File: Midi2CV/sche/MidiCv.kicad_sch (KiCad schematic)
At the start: 9 parts, among them U1 STM32F103C8T6_BD, U2 6N138

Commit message: re - revert
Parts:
- added U3: ~, symbol RetroElec:MCP4725_DAC_BD
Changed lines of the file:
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@@
+    )
+  )
+  (symbol (lib_id "RetroElec:MCP4725_DAC_BD") (at 195.58 54.61 0) (unit 1)
+    (in_bom yes) (on_board yes) (dnp no) (fields_autoplaced)
+    (property "Reference" "U3" (at 205.74 52.8292 0)
+      (effects (font (size 1.27 1.27)) (justify left))
+    )
+    (property "Value" "~" (at 194.31 52.07 0)
+      (effects (font (size 1.27 1.27)))
+    )
+    (property "Footprint" "" (at 194.31 52.07 0)
+      (effects (font (size 1.27 1.27)) hide)
+    )
+    (property "Datasheet" "" (at 194.31 52.07 0)
+      (effects (font (size 1.27 1.27)) hide)
+    )
+    (pin "")
+    (pin "")
+    (pin "")
+    (pin "")
+    (pin "")
+    (pin "")
+    (instances
+      (project "MidiCv"
+        (path "/0e81e7e9-28eb-4e3c-9e5d-03b0357b6be8"
+          (reference "U3") (unit 1)
+        )
+      )
     )
   )

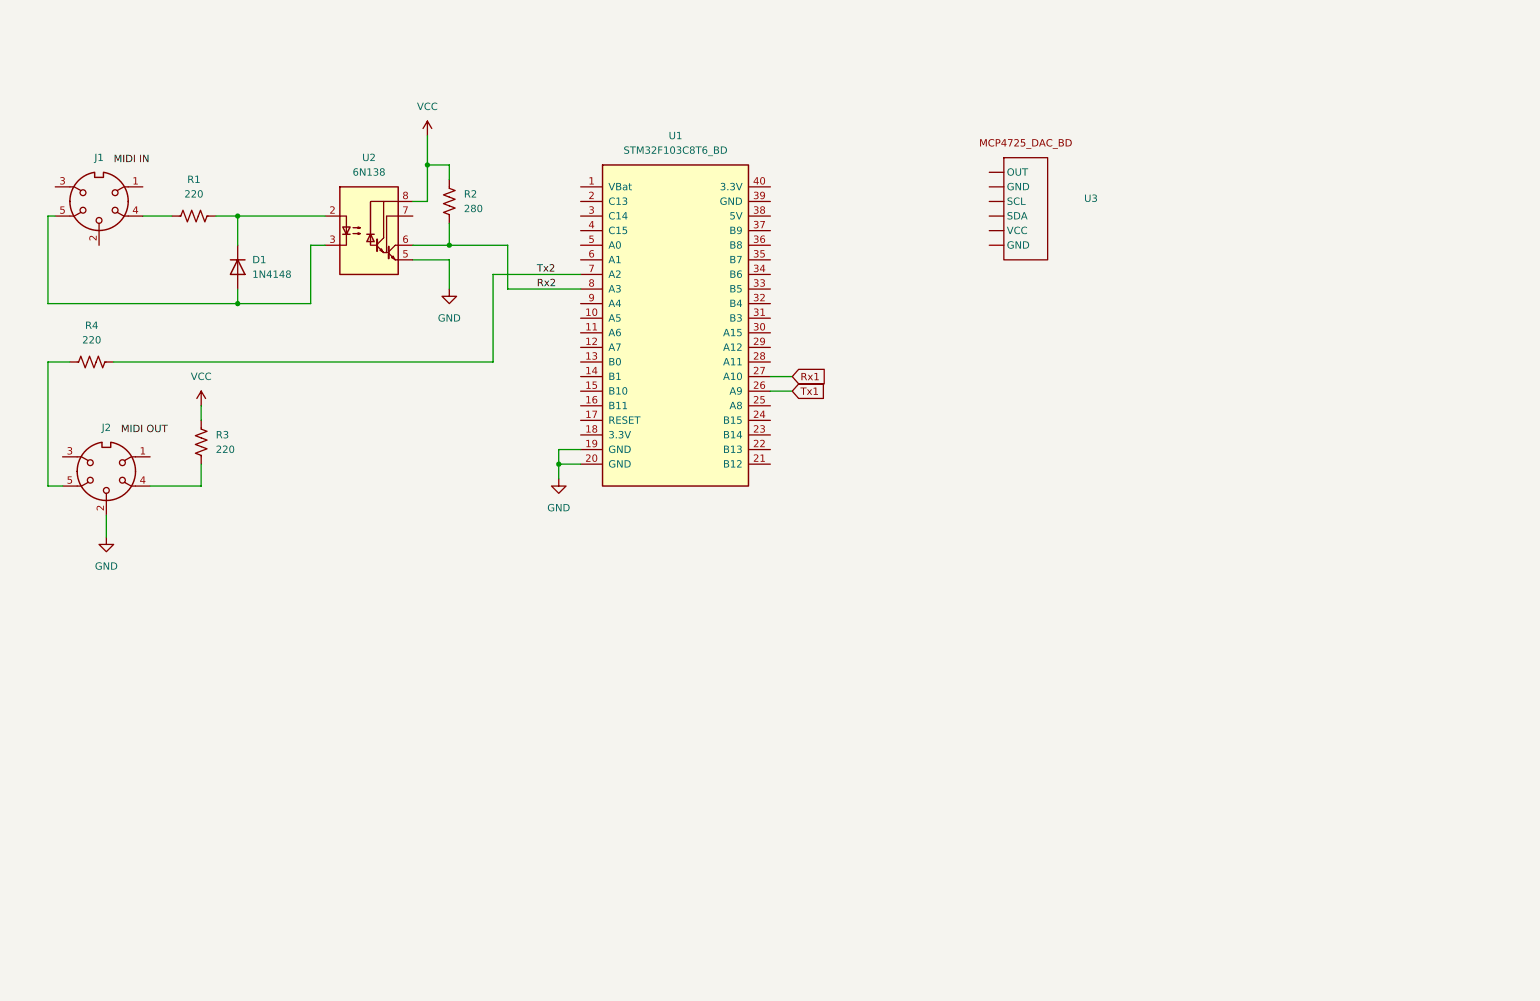
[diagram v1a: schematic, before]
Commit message: add i2c, A0_sel_pin
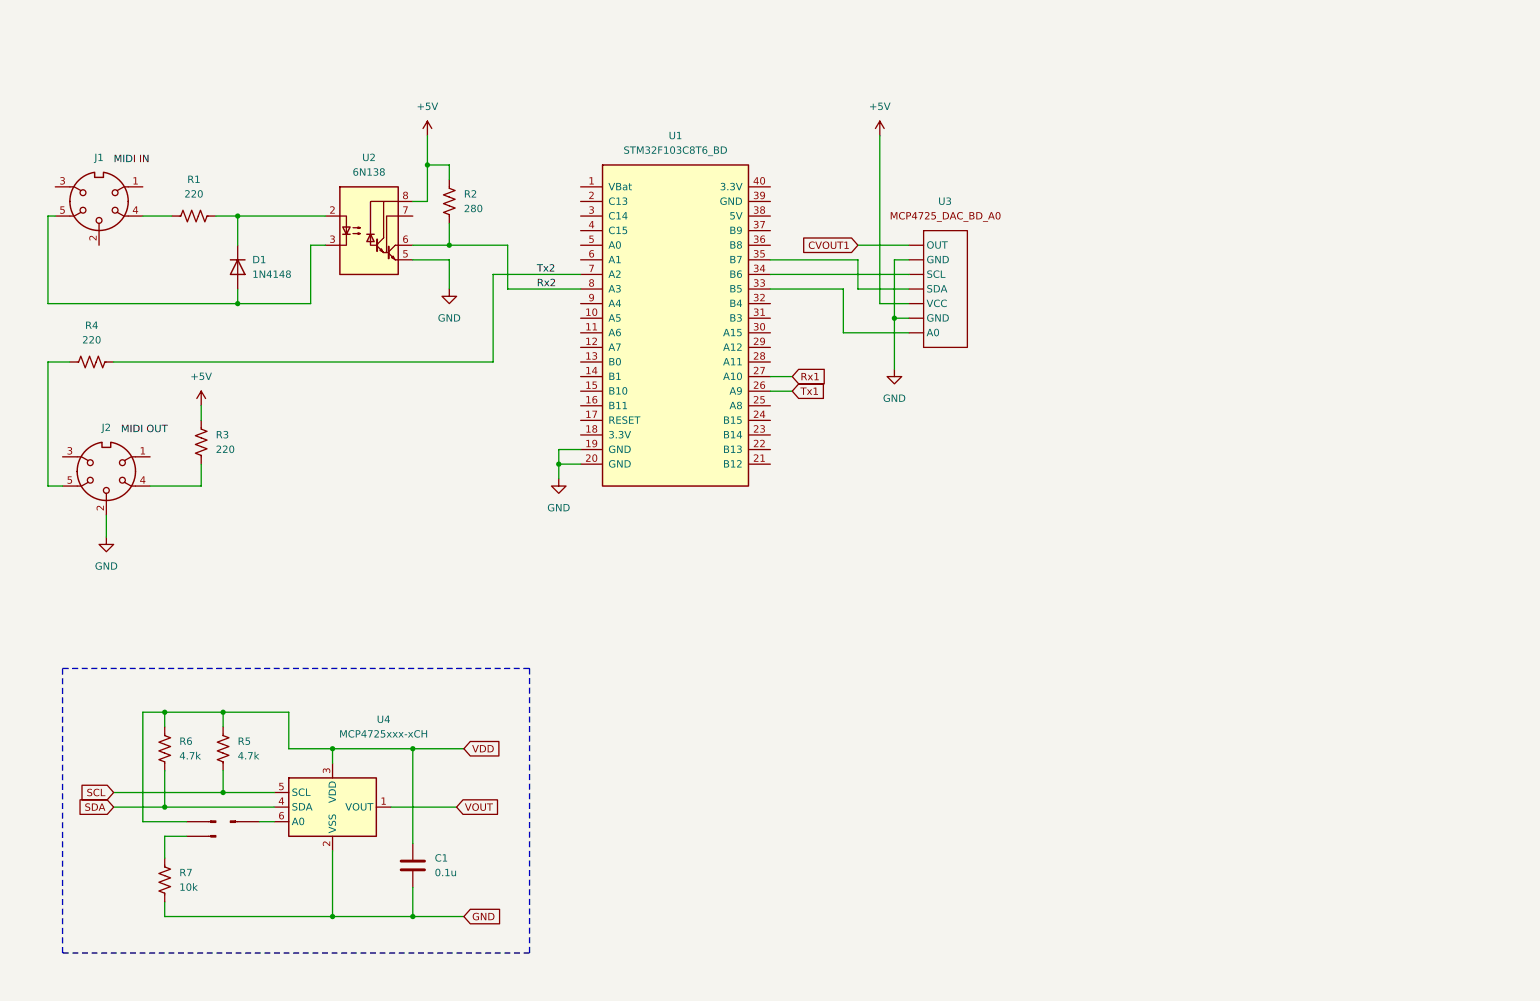
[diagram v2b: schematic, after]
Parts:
- removed U3: ~, symbol RetroElec:MCP4725_DAC_BD
- added C1: 0.1u, symbol Device:C
- added J3, J4, J5: Conn_01x01_Pin, symbol Connector:Conn_01x01_Pin
- added R5, R6: 4.7k, symbol Device:R_US
- added R7: 10k, symbol Device:R_US
- added U3: ~, symbol RetroElec:MCP4725_DAC_BD_A0
- added U4: MCP4725xxx-xCH, Package_TO_SOT_SMD:SOT-23-6, symbol Analog_DAC:MCP4725xxx-xCH
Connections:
- net GND: now also C1.2, R7.1, U3. (VCC), U4.2 (VSS)
- net at U1.33 (B5): now also U3. (VCC)
- net at U1.34 (B6): now also U3. (VCC)
- net at U1.35 (B7): now also U3. (VCC)
- net VCC renamed +5V
- net +5V: now also U3. (VCC)
- new net: J4.1 (Pin_1), U4.6 (A0)
- new net: J3.1 (Pin_1), R7.2
- new net CVOUT1: U3. (VCC)
- new net SCL: R5.1, U4.5 (SCL)
- new net SDA: R6.1, U4.4 (SDA)
- new net VDD: C1.1, J5.1 (Pin_1), R5.2, R6.2, U4.3 (VDD)
- new net VOUT: U4.1 (VOUT)

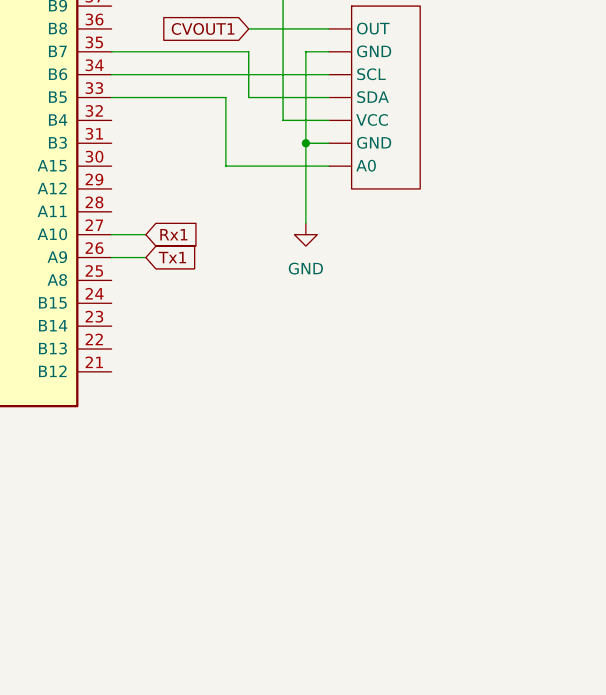
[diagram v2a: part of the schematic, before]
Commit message: - add set_CV function - add GATE control
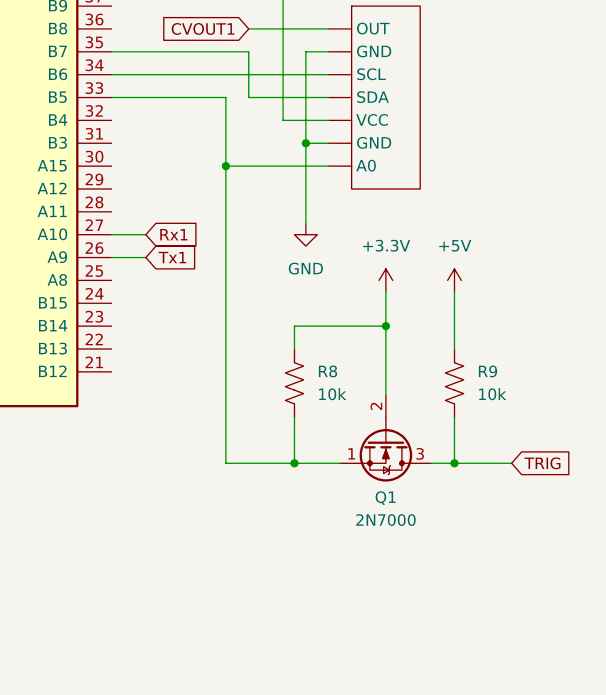
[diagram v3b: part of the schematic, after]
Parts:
- added Q1: 2N7000, Package_TO_SOT_THT:TO-92_Inline, symbol Transistor_FET:2N7000
- added R8, R9: 10k, symbol Device:R_US
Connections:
- net +5V: now also R9.2
- net at U1.33 (B5), U3. (VCC): now also Q1.1 (S), R8.1
- new net +3.3V: Q1.2 (G), R8.2
- new net TRIG: Q1.3 (D), R9.1
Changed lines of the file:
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@@
   (junction (at 74.93 148.59) (diameter 0) (color 0 0 0 0)
   )
+  (junction (at 181.61 93.98) (diameter 0) (color 0 0 0 0)
+  )
   (junction (at 55.88 142.24) (diameter 0) (color 0 0 0 0)
   )
@@
   (junction (at 91.44 46.99) (diameter 0) (color 0 0 0 0)
   )
+  (junction (at 163.83 76.2) (diameter 0) (color 0 0 0 0)
+  )
   (junction (at 74.93 177.8) (diameter 0) (color 0 0 0 0)
   )
@@
   (junction (at 45.72 142.24) (diameter 0) (color 0 0 0 0)
   )
+  (junction (at 171.45 109.22) (diameter 0) (color 0 0 0 0)
+  )
   (junction (at 172.72 73.66) (diameter 0) (color 0 0 0 0)
   )
@@
   (junction (at 114.3 99.06) (diameter 0) (color 0 0 0 0)
   )
+  (junction (at 189.23 109.22) (diameter 0) (color 0 0 0 0)
+  )
   (junction (at 45.72 158.75) (diameter 0) (color 0 0 0 0)
   )
@@
     (stroke (width 0) (type default))
   )
+  (wire (pts (xy 171.45 109.22) (xy 176.53 109.22))
+    (stroke (width 0) (type default))
+  )
   (wire (pts (xy 71.12 60.96) (xy 71.12 71.12))
     (stroke (width 0) (type default))
@@
     (stroke (width 0) (type default))
   )
+  (wire (pts (xy 181.61 90.17) (xy 181.61 93.98))
+    (stroke (width 0) (type default))
+  )
   (wire (pts (xy 95.25 60.96) (xy 95.25 57.15))
     (stroke (width 0) (type default))
@@
     (stroke (width 0) (type default))
   )
+  (wire (pts (xy 171.45 104.14) (xy 171.45 109.22))
+    (stroke (width 0) (type default))
+  )
+  (wire (pts (xy 189.23 104.14) (xy 189.23 109.22))
+    (stroke (width 0) (type default))
+  )
   (wire (pts (xy 95.25 63.5) (xy 95.25 68.58))
     (stroke (width 0) (type default))
   )
+  (wire (pts (xy 189.23 109.22) (xy 195.58 109.22))
+    (stroke (width 0) (type default))
+  )
   (wire (pts (xy 55.88 142.24) (xy 67.31 142.24))
     (stroke (width 0) (type default))
@@
     (stroke (width 0) (type default))
   )
+  (wire (pts (xy 181.61 93.98) (xy 181.61 101.6))
+    (stroke (width 0) (type default))
+  )
   (wire (pts (xy 175.26 63.5) (xy 172.72 63.5))
     (stroke (width 0) (type default))
@@
     (stroke (width 0) (type default))
   )
+  (wire (pts (xy 189.23 90.17) (xy 189.23 96.52))
+    (stroke (width 0) (type default))
+  )
   (wire (pts (xy 74.93 177.8) (xy 45.72 177.8))
     (stroke (width 0) (type default))
@@
     (stroke (width 0) (type default))
   )
+  (wire (pts (xy 163.83 76.2) (xy 175.26 76.2))
+    (stroke (width 0) (type default))
+  )
+  (wire (pts (xy 171.45 93.98) (xy 181.61 93.98))
+    (stroke (width 0) (type default))
+  )
+  (wire (pts (xy 171.45 96.52) (xy 171.45 93.98))
+    (stroke (width 0) (type default))
+  )
   (wire (pts (xy 43.18 102.87) (xy 52.07 102.87))
     (stroke (width 0) (type default))
@@
     (stroke (width 0) (type default))
   )
+  (wire (pts (xy 163.83 109.22) (xy 171.45 109.22))
+    (stroke (width 0) (type default))
+  )
   (wire (pts (xy 102.87 66.04) (xy 118.11 66.04))
     (stroke (width 0) (type default))
@@
     (stroke (width 0) (type default))
   )
+  (wire (pts (xy 186.69 109.22) (xy 189.23 109.22))
+    (stroke (width 0) (type default))
+  )
   (wire (pts (xy 166.37 68.58) (xy 175.26 68.58))
     (stroke (width 0) (type default))
@@
     (stroke (width 0) (type default))
   )
+  (wire (pts (xy 163.83 76.2) (xy 163.83 109.22))
+    (stroke (width 0) (type default))
+  )
   (wire (pts (xy 73.66 60.96) (xy 71.12 60.96))
     (stroke (width 0) (type default))
@@
   )
   (wire (pts (xy 45.72 163.83) (xy 49.53 163.83))
-    (stroke (width 0) (type default))
-  )
-  (wire (pts (xy 163.83 76.2) (xy 175.26 76.2))
     (stroke (width 0) (type default))
   )
@@
     )
   )
+  (global_label "TRIG" (shape input) (at 195.58 109.22 0) (fields_autoplaced)
+    (effects (font (size 1.27 1.27)) (justify left))
+    (property "Intersheetrefs" "${INTERSHEET_REFS}" (at 202.6776 109.22 0)
+      (effects (font (size 1.27 1.27)) (justify left) hide)
+    )
+  )
   (symbol (lib_id "power:GND") (at 172.72 82.55 0) (unit 1)
     (in_bom yes) (on_board yes) (dnp no) (fields_autoplaced)
@@
         (path "/0e81e7e9-28eb-4e3c-9e5d-03b0357b6be8"
           (reference "#PWR06") (unit 1)
+        )
+      )
+    )
+  )
+  (symbol (lib_id "power:+5V") (at 189.23 90.17 0) (unit 1)
+    (in_bom yes) (on_board yes) (dnp no) (fields_autoplaced)
+    (property "Reference" "#PWR08" (at 189.23 93.98 0)
+      (effects (font (size 1.27 1.27)) hide)
+    )
+    (property "Value" "+5V" (at 189.23 85.09 0)
+      (effects (font (size 1.27 1.27)))
+    )
+    (property "Footprint" "" (at 189.23 90.17 0)
+      (effects (font (size 1.27 1.27)) hide)
+    )
+    (property "Datasheet" "" (at 189.23 90.17 0)
+      (effects (font (size 1.27 1.27)) hide)
+    )
+    (pin "1")
+    (instances
+      (project "MidiCv"
+        (path "/0e81e7e9-28eb-4e3c-9e5d-03b0357b6be8"
+          (reference "#PWR08") (unit 1)
         )
       )
@@
     )
   )
+  (symbol (lib_id "Device:R_US") (at 189.23 100.33 180) (unit 1)
+    (in_bom yes) (on_board yes) (dnp no) (fields_autoplaced)
+    (property "Reference" "R9" (at 191.77 99.06 0)
+      (effects (font (size 1.27 1.27)) (justify right))
+    )
+    (property "Value" "10k" (at 191.77 101.6 0)
+      (effects (font (size 1.27 1.27)) (justify right))
+    )
+    (property "Footprint" "" (at 188.214 100.076 90)
+      (effects (font (size 1.27 1.27)) hide)
+    )
+    (property "Datasheet" "~" (at 189.23 100.33 0)
+      (effects (font (size 1.27 1.27)) hide)
+    )
+    (pin "1")
+    (pin "2")
+    (instances
+      (project "MidiCv"
+        (path "/0e81e7e9-28eb-4e3c-9e5d-03b0357b6be8"
+          (reference "R9") (unit 1)
+        )
+      )
+    )
+  )
   (symbol (lib_id "power:GND") (at 35.56 111.76 0) (unit 1)
     (in_bom yes) (on_board yes) (dnp no) (fields_autoplaced)
@@
         (path "/0e81e7e9-28eb-4e3c-9e5d-03b0357b6be8"
           (reference "#PWR05") (unit 1)
+        )
+      )
+    )
+  )
+  (symbol (lib_id "power:+3.3V") (at 181.61 90.17 0) (unit 1)
+    (in_bom yes) (on_board yes) (dnp no) (fields_autoplaced)
+    (property "Reference" "#PWR09" (at 181.61 93.98 0)
+      (effects (font (size 1.27 1.27)) hide)
+    )
+    (property "Value" "+3.3V" (at 181.61 85.09 0)
+      (effects (font (size 1.27 1.27)))
+    )
+    (property "Footprint" "" (at 181.61 90.17 0)
+      (effects (font (size 1.27 1.27)) hide)
+    )
+    (property "Datasheet" "" (at 181.61 90.17 0)
+      (effects (font (size 1.27 1.27)) hide)
+    )
+    (pin "1")
+    (instances
+      (project "MidiCv"
+        (path "/0e81e7e9-28eb-4e3c-9e5d-03b0357b6be8"
+          (reference "#PWR09") (unit 1)
         )
       )
@@
         (path "/0e81e7e9-28eb-4e3c-9e5d-03b0357b6be8"
           (reference "#PWR02") (unit 1)
+        )
+      )
+    )
+  )
+  (symbol (lib_id "Transistor_FET:2N7000") (at 181.61 106.68 270) (unit 1)
+    (in_bom yes) (on_board yes) (dnp no) (fields_autoplaced)
+    (property "Reference" "Q1" (at 181.61 113.03 90)
+      (effects (font (size 1.27 1.27)))
+    )
+    (property "Value" "2N7000" (at 181.61 115.57 90)
+      (effects (font (size 1.27 1.27)))
+    )
+    (property "Footprint" "Package_TO_SOT_THT:TO-92_Inline" (at 179.705 111.76 0)
+      (effects (font (size 1.27 1.27) italic) (justify left) hide)
+    )
+    (property "Datasheet" "https://www.vishay.com/docs/70226/70226.pdf" (at 181.61 106.68 0)
+      (effects (font (size 1.27 1.27)) (justify left) hide)
+    )
+    (pin "1")
+    (pin "3")
+    (pin "2")
+    (instances
+      (project "MidiCv"
+        (path "/0e81e7e9-28eb-4e3c-9e5d-03b0357b6be8"
+          (reference "Q1") (unit 1)
         )
       )
@@
         )
       )
+    )
+  )
+  (symbol (lib_id "Device:R_US") (at 171.45 100.33 180) (unit 1)
+    (in_bom yes) (on_board yes) (dnp no) (fields_autoplaced)
+    (property "Reference" "R8" (at 173.99 99.06 0)
+      (effects (font (size 1.27 1.27)) (justify right))
+    )
+    (property "Value" "10k" (at 173.99 101.6 0)
+      (effects (font (size 1.27 1.27)) (justify right))
+    )
+    (property "Footprint" "" (at 170.434 100.076 90)
+      (effects (font (size 1.27 1.27)) hide)
+    )
+    (property "Datasheet" "~" (at 171.45 100.33 0)
+      (effects (font (size 1.27 1.27)) hide)
+    )
+    (pin "1")
+    (pin "2")
+    (instances
+      (project "MidiCv"
+        (path "/0e81e7e9-28eb-4e3c-9e5d-03b0357b6be8"
+          (reference "R8") (unit 1)
+        )
+      )
